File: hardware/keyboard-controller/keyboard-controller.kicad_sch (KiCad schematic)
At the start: 8 parts, among them J1 Debug_Pins, SW1 RESET, SW2 MODE_SEL, U1 Pico, U2 MCP4921

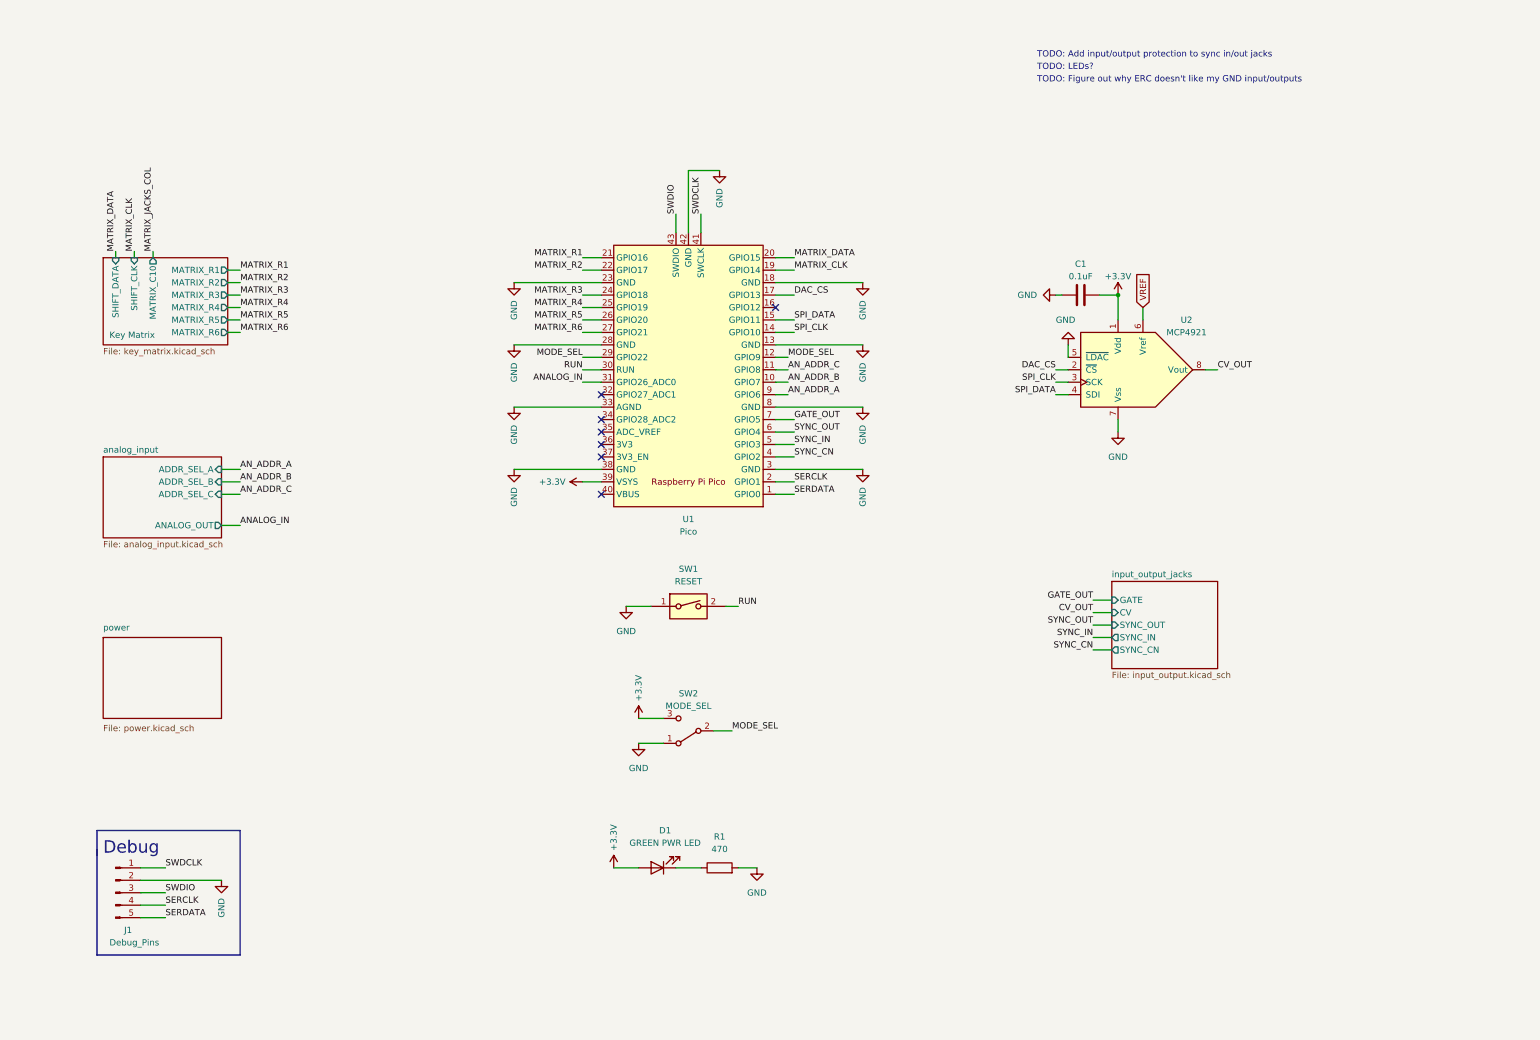
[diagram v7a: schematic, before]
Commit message: Updated hardware_config and fixed sync_cn
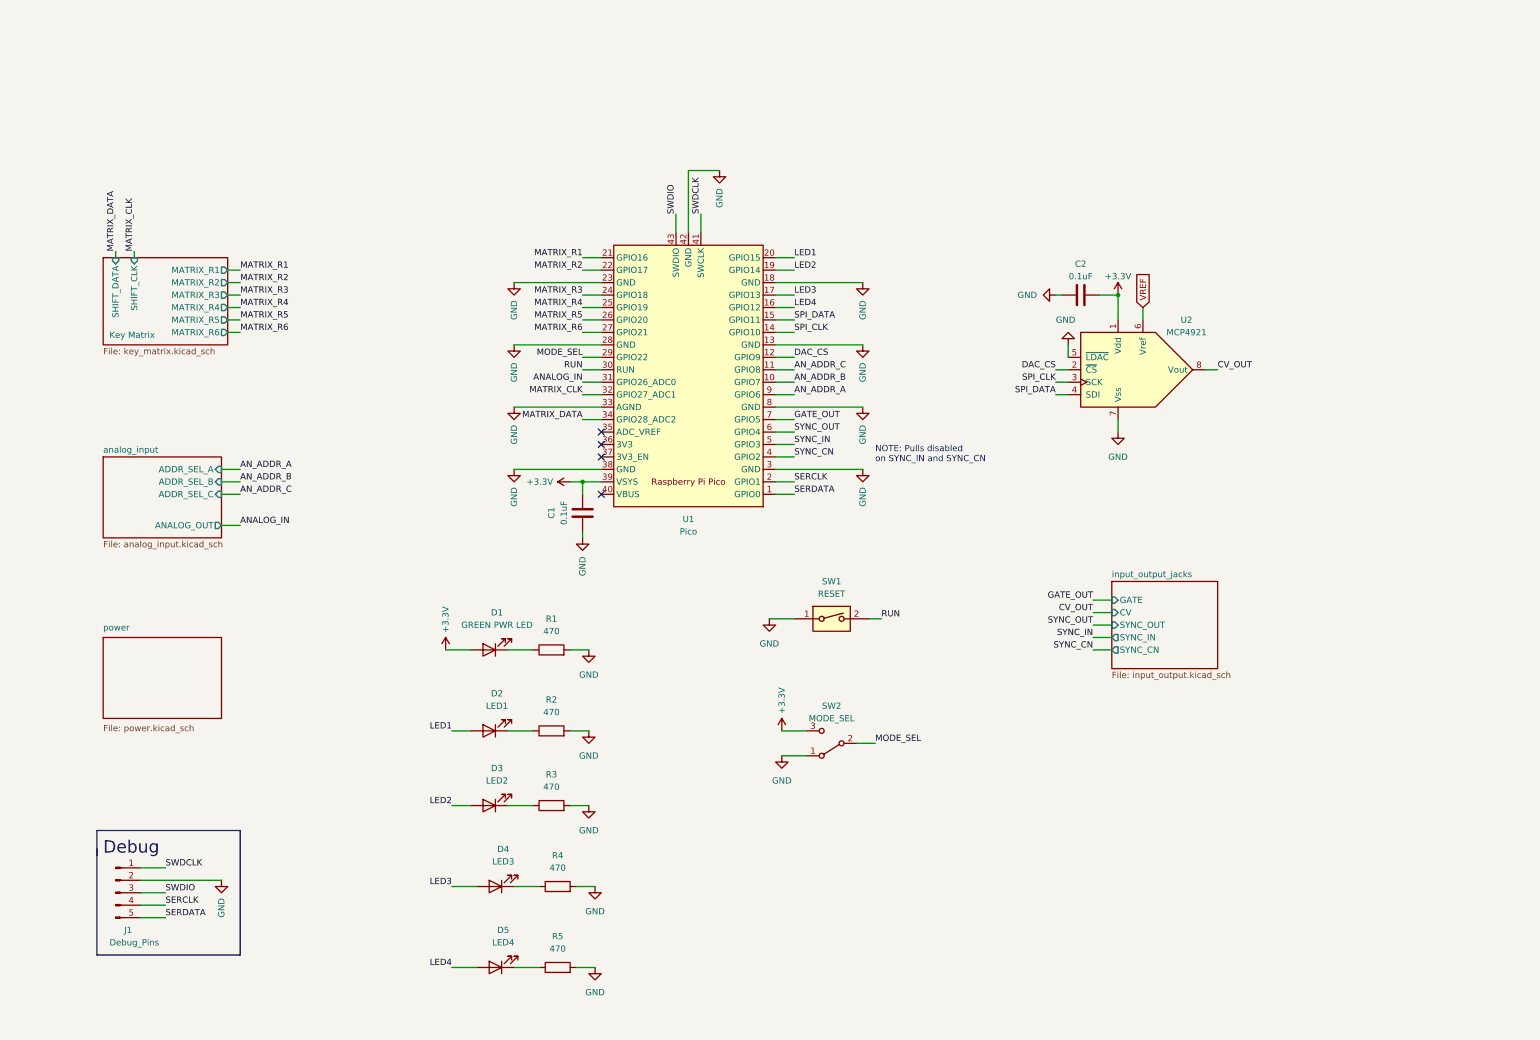
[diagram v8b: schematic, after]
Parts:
- added C1: 0.1uF, AEC_Capacitors:C_Disc_D5.0mm_W2.5mm_P3.0mm, symbol Device:C
- added D2: LED1, symbol Device:LED
- added D3: LED2, symbol Device:LED
- added D4: LED3, symbol Device:LED
- added D5: LED4, symbol Device:LED
- added R2, R3, R4, R5: 470, symbol Device:R
- C2: renamed from C1; Notes (none) -> Ceramic
- D1, R1, SW1: Supplier (none) -> Tayda
- U1: footprint MCU_RaspberryPi_and_Boards:RPi_Pico_SMD_TH -> RPi_Pico:RPi_Pico_SMD_TH
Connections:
- net +3V3: now also C1.2
- net DAC_CS: now also U1.12 (GPIO9); no longer U1.17 (GPIO13)
- net GND: now also C1.1, R2.2, R3.2, R4.2, R5.2
- net MATRIX_CLK: now also U1.32 (GPIO27_ADC1); no longer U1.19 (GPIO14)
- net MATRIX_DATA: now also U1.34 (GPIO28_ADC2); no longer U1.20 (GPIO15)
- net MODE_SEL: no longer U1.12 (GPIO9)
- net LED4: now reaches U1.16 (GPIO12)
- net LED4: now also D5.2 (A)
- new net: D4.1 (K), R4.1
- new net: D2.1 (K), R2.1
- new net: D5.1 (K), R5.1
- new net: D3.1 (K), R3.1
- new net LED1: D2.2 (A), U1.20 (GPIO15)
- new net LED2: D3.2 (A), U1.19 (GPIO14)
- new net LED3: D4.2 (A), U1.17 (GPIO13)
- no-connect marks 7 -> 4
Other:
- sheet Key Matrix ports: added none; removed MATRIX_C10
- note added: "NOTE: Pulls disabled on SYNC_IN and SYNC_CN"
- note removed: "TODO: Add input/output protection to sync in/out jacks"
- note removed: "TODO: Figure out why ERC doesn't like my GND input/outputs"
- note removed: "TODO: LEDs?"
- moved on the sheet: D1, R1, SW1, SW2
